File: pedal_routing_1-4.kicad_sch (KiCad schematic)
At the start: 14 parts, among them U501 CD4051B, U502 CD4051B, U503 CD4051B, U504 CD4051B

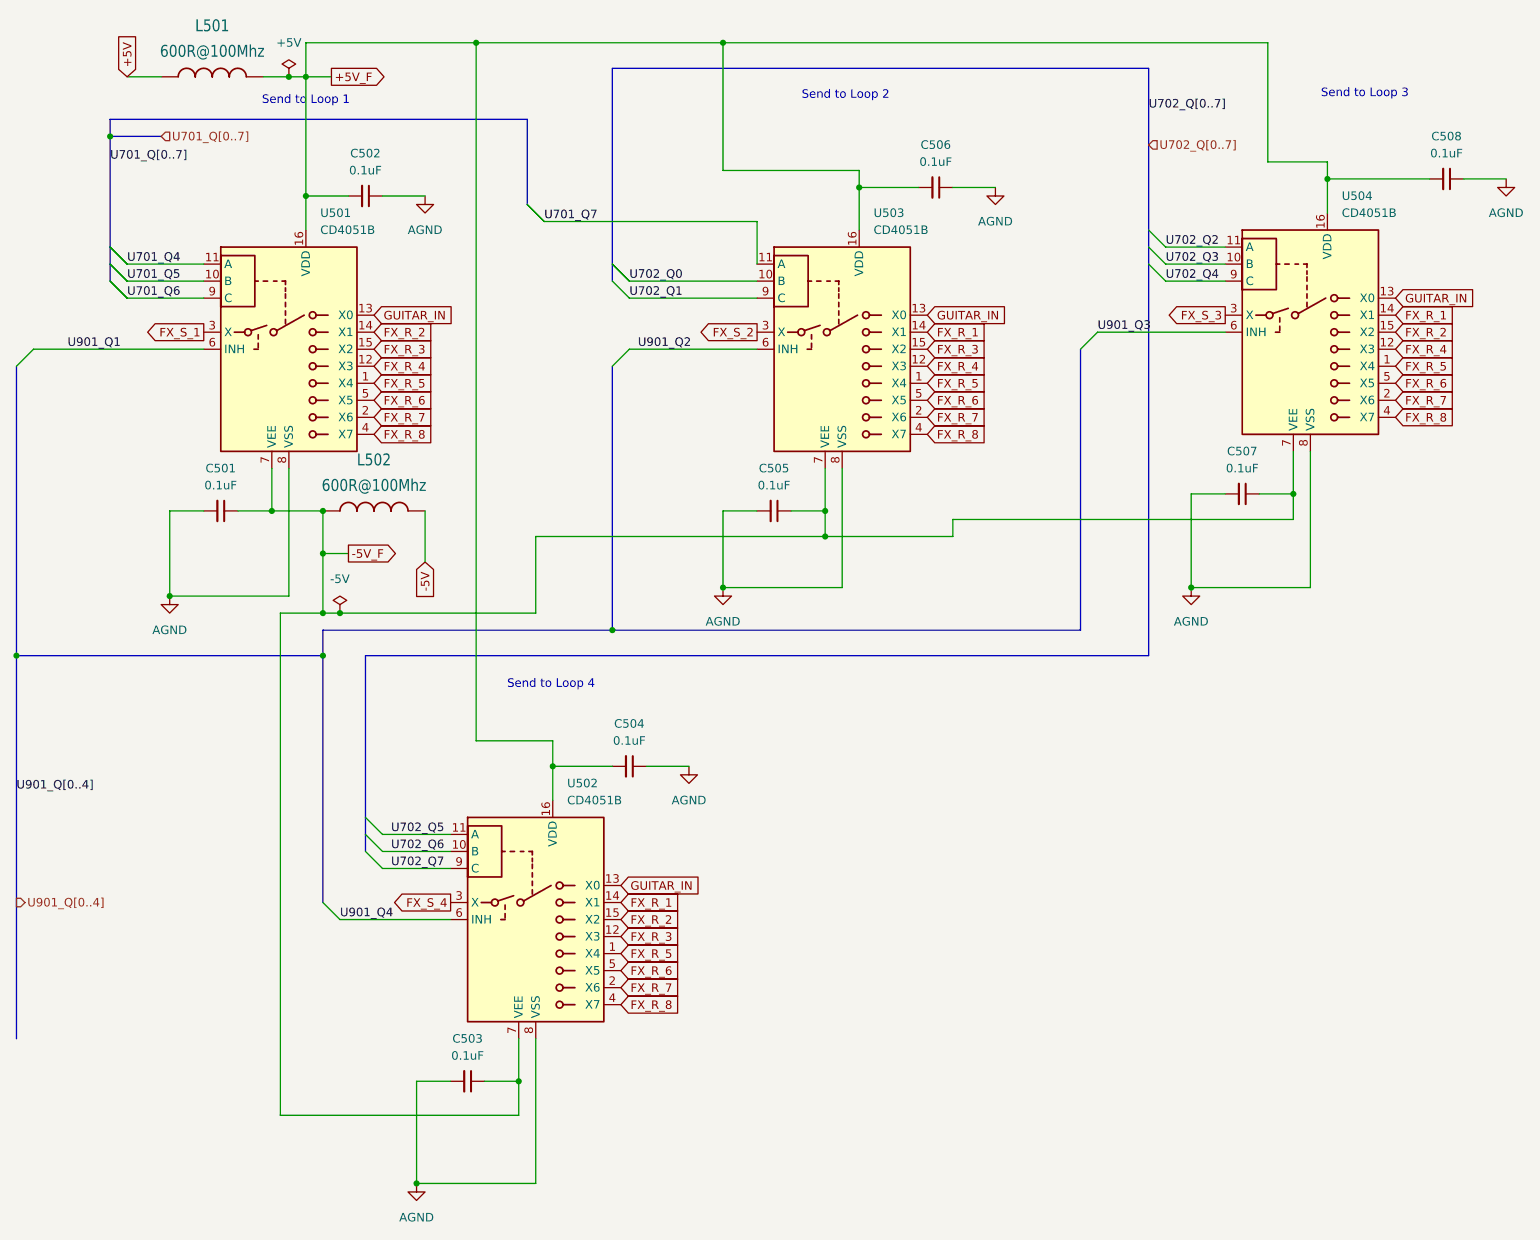
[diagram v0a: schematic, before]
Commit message: Removed un-needed inhibit from amp out. thereby simplifying the shift registers.
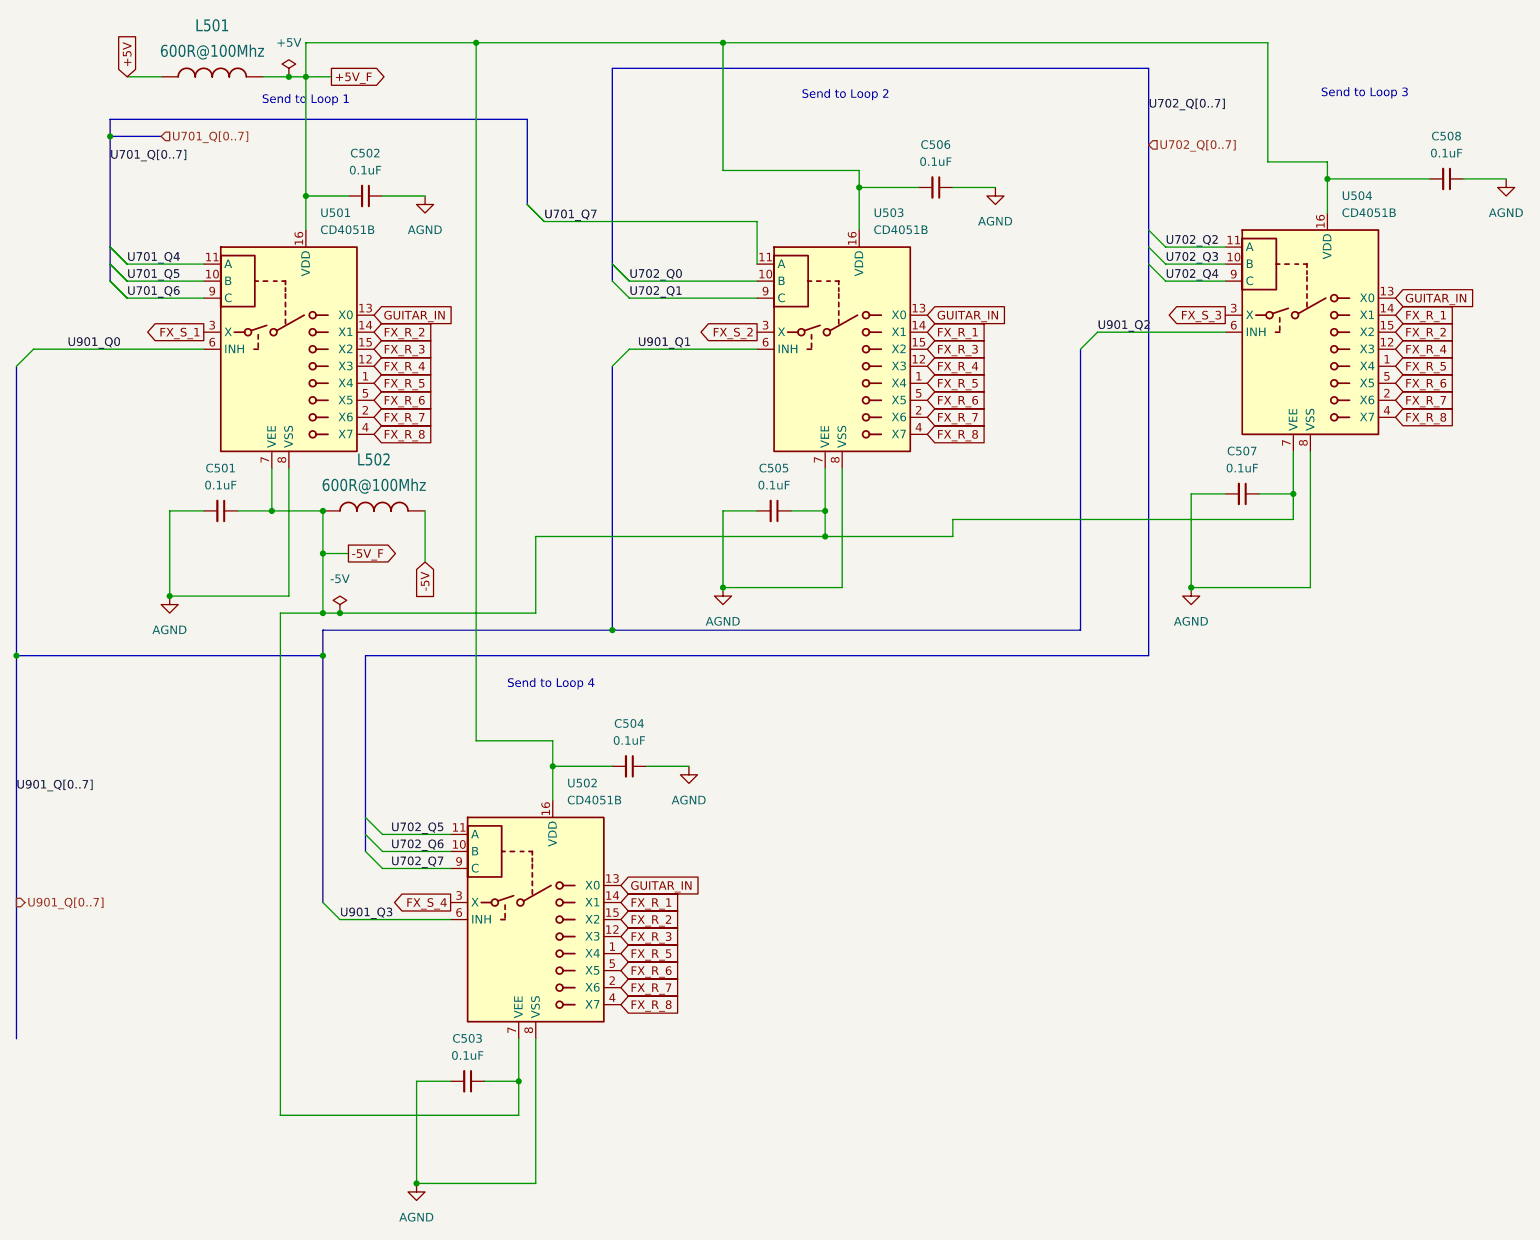
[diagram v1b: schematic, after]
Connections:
- net U901_Q4 is gone; now on net U901_Q3: U502.6 (INH)
- net U901_Q1: now also U503.6 (INH); no longer U501.6 (INH)
- net U901_Q2: now also U504.6 (INH); no longer U503.6 (INH)
- net U901_Q3: no longer U504.6 (INH)
- new net U901_Q0: U501.6 (INH)
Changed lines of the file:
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@@
 		)
 	)
-	(label "U901_Q[0..4]"
+	(label "U901_Q[0..7]"
 		(at 29.21 125.73 0)
 		(effects
@@
 		)
 	)
-	(label "U901_Q2"
+	(label "U901_Q1"
 		(at 121.92 59.69 0)
 		(effects
@@
 		)
 	)
-	(label "U901_Q1"
+	(label "U901_Q0"
 		(at 36.83 59.69 0)
 		(effects
@@
 		)
 	)
-	(label "U901_Q4"
+	(label "U901_Q3"
 		(at 77.47 144.78 0)
 		(effects
@@
 		)
 	)
-	(label "U901_Q3"
+	(label "U901_Q2"
 		(at 190.5 57.15 0)
 		(effects
@@
 		)
 	)
-	(hierarchical_label "U901_Q[0..4]"
+	(hierarchical_label "U901_Q[0..7]"
 		(shape output)
 		(at 29.21 142.24 0)

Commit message: Removed LED Shift registers and replaced them with PCA9685 PWM controllers, Also changed LEDs to RGB LEDs.
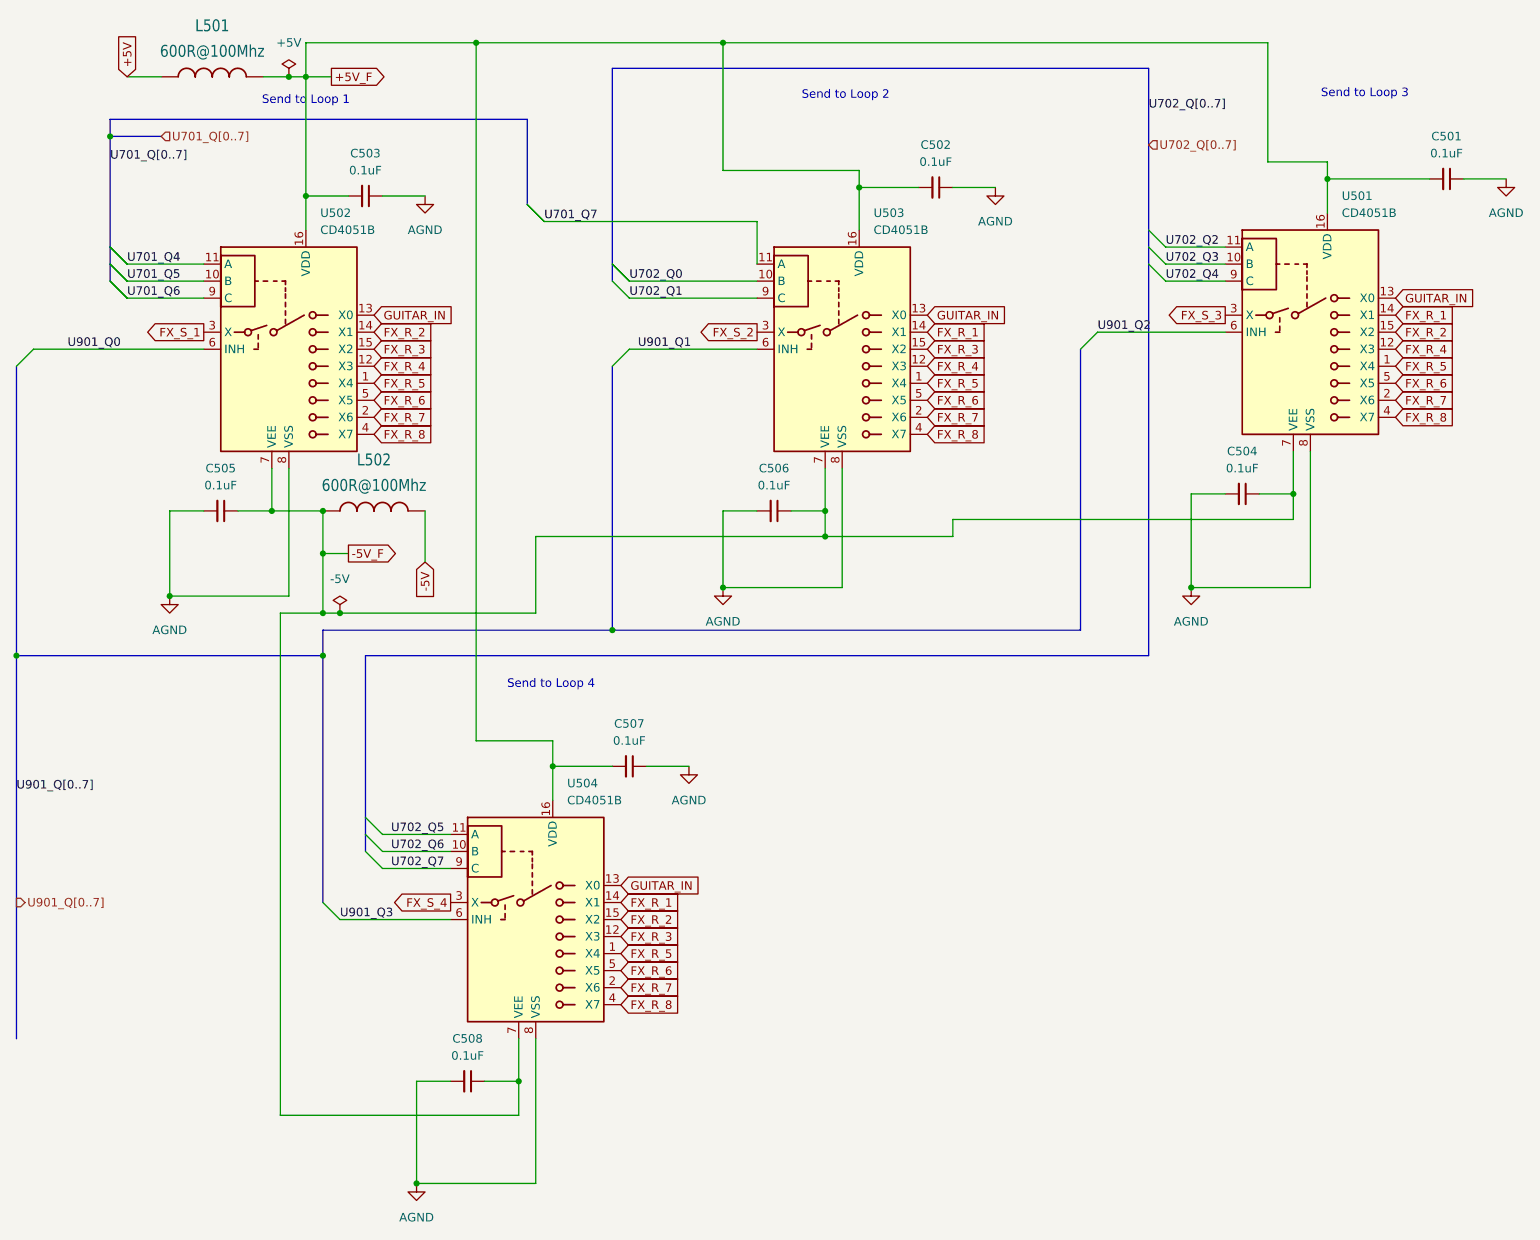
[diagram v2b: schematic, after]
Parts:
- renumbered C508 to C501, C506 to C502, C502 to C503, C507 to C504, C501 to C505, C505 to C506, C504 to C507, C503 to C508, U504 to U501, U501 to U502, U502 to U504
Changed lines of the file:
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@@
 		(on_board yes)
 		(dnp no)
-		(property "Reference" "#PWR0501"
+		(property "Reference" "#PWR0506"
 			(at 52.07 102.87 0)
 			(effects
@@
 			(project "circuit"
 				(path "/420e3d7a-6c9a-4806-b4be-05d56aeb21de/be7f89fe-51f3-4dfc-9362-b897b38bc33a"
-					(reference "#PWR0501")
+					(reference "#PWR0506")
 					(unit 1)
 				)
@@
 		(on_board yes)
 		(dnp no)
-		(property "Reference" "#PWR0504"
+		(property "Reference" "#PWR0507"
 			(at 129.54 128.27 0)
 			(effects
@@
 			(project "circuit"
 				(path "/420e3d7a-6c9a-4806-b4be-05d56aeb21de/be7f89fe-51f3-4dfc-9362-b897b38bc33a"
-					(reference "#PWR0504")
+					(reference "#PWR0507")
 					(unit 1)
 				)
@@
 		(on_board yes)
 		(dnp no)
-		(property "Reference" "#PWR0506"
+		(property "Reference" "#PWR0502"
 			(at 175.26 41.91 0)
 			(effects
@@
 			(project "circuit"
 				(path "/420e3d7a-6c9a-4806-b4be-05d56aeb21de/be7f89fe-51f3-4dfc-9362-b897b38bc33a"
-					(reference "#PWR0506")
+					(reference "#PWR0502")
 					(unit 1)
 				)
@@
 		(dnp no)
 		(fields_autoplaced yes)
-		(property "Reference" "U504"
+		(property "Reference" "U501"
 			(at 226.9333 36.83 0)
 			(effects
@@
 			(project "circuit"
 				(path "/420e3d7a-6c9a-4806-b4be-05d56aeb21de/be7f89fe-51f3-4dfc-9362-b897b38bc33a"
-					(reference "U504")
+					(reference "U501")
 					(unit 1)
 				)
@@
 		(on_board yes)
 		(dnp no)
-		(property "Reference" "#PWR0505"
+		(property "Reference" "#PWR0504"
 			(at 134.62 101.6 0)
 			(effects
@@
 			(project "circuit"
 				(path "/420e3d7a-6c9a-4806-b4be-05d56aeb21de/be7f89fe-51f3-4dfc-9362-b897b38bc33a"
-					(reference "#PWR0505")
+					(reference "#PWR0504")
 					(unit 1)
 				)
@@
 		(dnp no)
 		(fields_autoplaced yes)
-		(property "Reference" "C506"
+		(property "Reference" "C502"
 			(at 166.3636 29.21 90)
 			(effects
@@
 			(project "circuit"
 				(path "/420e3d7a-6c9a-4806-b4be-05d56aeb21de/be7f89fe-51f3-4dfc-9362-b897b38bc33a"
-					(reference "C506")
+					(reference "C502")
 					(unit 1)
 				)
@@
 		(on_board yes)
 		(dnp no)
-		(property "Reference" "#PWR0502"
+		(property "Reference" "#PWR0508"
 			(at 88.9 190.5 0)
 			(effects
@@
 			(project "circuit"
 				(path "/420e3d7a-6c9a-4806-b4be-05d56aeb21de/be7f89fe-51f3-4dfc-9362-b897b38bc33a"
-					(reference "#PWR0502")
+					(reference "#PWR0508")
 					(unit 1)
 				)
@@
 		(dnp no)
 		(fields_autoplaced yes)
-		(property "Reference" "C505"
+		(property "Reference" "C506"
 			(at 142.2336 77.47 90)
 			(effects
@@
 			(project "circuit"
 				(path "/420e3d7a-6c9a-4806-b4be-05d56aeb21de/be7f89fe-51f3-4dfc-9362-b897b38bc33a"
-					(reference "C505")
+					(reference "C506")
 					(unit 1)
 				)
@@
 		(on_board yes)
 		(dnp no)
-		(property "Reference" "#PWR0507"
+		(property "Reference" "#PWR0505"
 			(at 204.47 101.6 0)
 			(effects
@@
 			(project "circuit"
 				(path "/420e3d7a-6c9a-4806-b4be-05d56aeb21de/be7f89fe-51f3-4dfc-9362-b897b38bc33a"
-					(reference "#PWR0507")
+					(reference "#PWR0505")
 					(unit 1)
 				)
@@
 		(on_board yes)
 		(dnp no)
-		(property "Reference" "#PWR0508"
+		(property "Reference" "#PWR0501"
 			(at 251.46 40.64 0)
 			(effects
@@
 			(project "circuit"
 				(path "/420e3d7a-6c9a-4806-b4be-05d56aeb21de/be7f89fe-51f3-4dfc-9362-b897b38bc33a"
-					(reference "#PWR0508")
+					(reference "#PWR0501")
 					(unit 1)
 				)
@@
 		(dnp no)
 		(fields_autoplaced yes)
-		(property "Reference" "U501"
+		(property "Reference" "U502"
 			(at 74.5333 39.37 0)
 			(effects
@@
 			(project "circuit"
 				(path "/420e3d7a-6c9a-4806-b4be-05d56aeb21de/be7f89fe-51f3-4dfc-9362-b897b38bc33a"
-					(reference "U501")
+					(reference "U502")
 					(unit 1)
 				)
@@
 		(dnp no)
 		(fields_autoplaced yes)
-		(property "Reference" "C504"
+		(property "Reference" "C507"
 			(at 120.6436 115.57 90)
 			(effects
@@
 			(project "circuit"
 				(path "/420e3d7a-6c9a-4806-b4be-05d56aeb21de/be7f89fe-51f3-4dfc-9362-b897b38bc33a"
-					(reference "C504")
+					(reference "C507")
 					(unit 1)
 				)
@@
 		(on_board yes)
 		(dnp no)
-		(property "Reference" "U502"
+		(property "Reference" "U504"
 			(at 111.3633 124.46 0)
 			(effects
@@
 			(project "circuit"
 				(path "/420e3d7a-6c9a-4806-b4be-05d56aeb21de/be7f89fe-51f3-4dfc-9362-b897b38bc33a"
-					(reference "U502")
+					(reference "U504")
 					(unit 1)
 				)
@@
 		(dnp no)
 		(fields_autoplaced yes)
-		(property "Reference" "C501"
+		(property "Reference" "C505"
 			(at 59.6836 77.47 90)
 			(effects
@@
 			(project ""
 				(path "/420e3d7a-6c9a-4806-b4be-05d56aeb21de/be7f89fe-51f3-4dfc-9362-b897b38bc33a"
-					(reference "C501")
+					(reference "C505")
 					(unit 1)
 				)
@@
 		(dnp no)
 		(fields_autoplaced yes)
-		(property "Reference" "C502"
+		(property "Reference" "C503"
 			(at 81.2736 30.48 90)
 			(effects
@@
 			(project "circuit"
 				(path "/420e3d7a-6c9a-4806-b4be-05d56aeb21de/be7f89fe-51f3-4dfc-9362-b897b38bc33a"
-					(reference "C502")
+					(reference "C503")
 					(unit 1)
 				)
@@
 		(dnp no)
 		(fields_autoplaced yes)
-		(property "Reference" "C503"
+		(property "Reference" "C508"
 			(at 96.5136 162.56 90)
 			(effects
@@
 			(project "circuit"
 				(path "/420e3d7a-6c9a-4806-b4be-05d56aeb21de/be7f89fe-51f3-4dfc-9362-b897b38bc33a"
-					(reference "C503")
+					(reference "C508")
 					(unit 1)
 				)
@@
 		(dnp no)
 		(fields_autoplaced yes)
-		(property "Reference" "C508"
+		(property "Reference" "C501"
 			(at 242.5636 27.94 90)
 			(effects
@@
 			(project "circuit"
 				(path "/420e3d7a-6c9a-4806-b4be-05d56aeb21de/be7f89fe-51f3-4dfc-9362-b897b38bc33a"
-					(reference "C508")
+					(reference "C501")
 					(unit 1)
 				)
@@
 		(dnp no)
 		(fields_autoplaced yes)
-		(property "Reference" "C507"
+		(property "Reference" "C504"
 			(at 212.0836 74.93 90)
 			(effects
@@
 			(project "circuit"
 				(path "/420e3d7a-6c9a-4806-b4be-05d56aeb21de/be7f89fe-51f3-4dfc-9362-b897b38bc33a"
-					(reference "C507")
-					(unit 1)
-				)
+					(reference "C504")
+					(unit 1)
+				)
